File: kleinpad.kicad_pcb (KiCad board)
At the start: 2 copper layers, 25 parts, among them J1 Conn_01x02, J2 Conn_01x05, SW1 SW_Push, SW2 RotaryEncoder_Switch, U1 SuperMini nRF52840

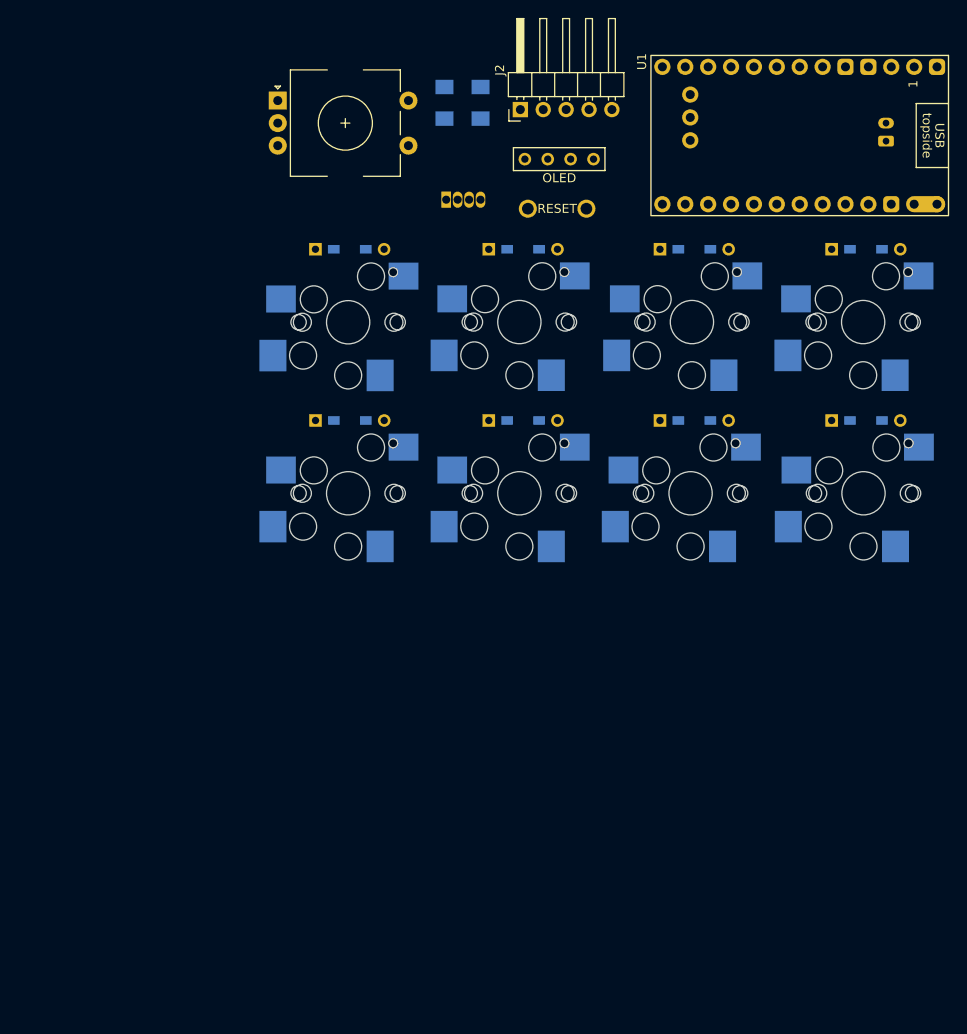
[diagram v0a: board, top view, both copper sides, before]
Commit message: feat: 回路図を追加
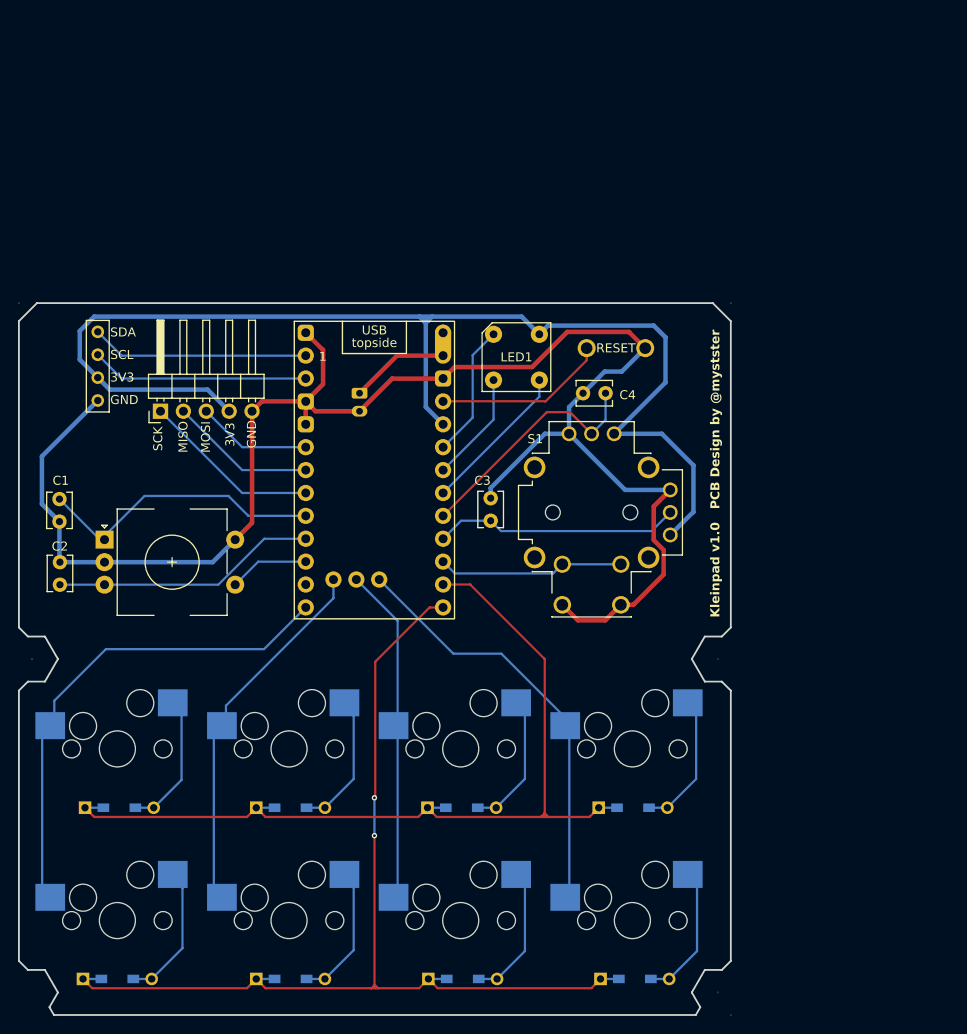
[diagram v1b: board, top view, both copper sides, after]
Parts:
- removed D9: LED_ABGR, LED_THT:LED_D5.0mm-4_RGB
- added C3: 0.1u, Capacitor_THT:C_Disc_D3.8mm_W2.6mm_P2.50mm, F.Cu at (153.6, 84.6)
- added C4: 0.1u, Capacitor_THT:C_Disc_D3.8mm_W2.6mm_P2.50mm, F.Cu at (166.4, 70.5)
- added LED1: LED_ABGR, myLibrary:LED Rectangle(OSTBMAZ2C1D), F.Cu at (156.5, 66.5)
- added S1: RKJXV122400R, RKJXV122400R:SW_RKJXV122400R, F.Cu at (164.8, 83.7)
- C1, C2: footprint kbd_Parts:Capacitor_1206 -> Capacitor_THT:C_Disc_D3.8mm_W2.6mm_P2.50mm; moved to F.Cu
- RC1-1, RC1-2, RC2-1, RC2-2, RC3-1, RC3-2, RC4-1, RC4-2: footprint kbd_SW_PCBA:MX_Choc_v1v2_Hotswap_1u -> kbd_SW:CherryMX_Hotswap_1u; moved to F.Cu
- moved C2 68.3 mm to (105.8, 91.7), turned to 90 degrees
- moved D7 67.2 mm to (169.4, 116.5)
- moved D2 67.1 mm to (112.2, 135.5)
- moved D4 67.1 mm to (131.4, 135.5)
- moved D3 67.1 mm to (131.4, 116.5)
- moved D5 67.1 mm to (150.4, 116.5)
- moved D6 67.1 mm to (150.5, 135.5)
- moved D8 67.1 mm to (169.6, 135.5)
- moved D1 67.0 mm to (112.4, 116.5)
- moved C1 65.8 mm to (105.8, 84.7), turned to 90 degrees
- moved J1 64.8 mm to (139.1, 70.5), turned to -90 degrees
- moved U1 59.9 mm to (140.7, 80.3), turned to 0 degrees
- moved OL1 58.3 mm to (110.0, 63.7), turned to -90 degrees
- moved RC4-2 53.9 mm to (169.4, 129.0), turned to 0 degrees
- moved RC1-2 53.9 mm to (112.2, 129.0), turned to 0 degrees
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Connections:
- U1 pad 10: LED_R -> RE_SW
- U1 pad 11: LED_G -> unconnected-(U1-P1.04-LF-Pad11)
- U1 pad 12: LED_B -> COL_1
- U1 pad 17: ROW_1 -> LED_R
- U1 pad 18: ROW_2 -> LED_G
- U1 pad 19: unconnected-(U1-P0.02-LF-Pad19) -> LED_B
- U1 pad 20: COL_4 -> JOY_Y
- U1 pad 21: COL_3 -> JOY_X
- U1 pad 22: COL_2 -> JOY_SW
- U1 pad 23: COL_1 -> ROW_1
- U1 pad 24: RE_SW -> ROW_2
- U1 pad 25: unconnected-(U1-P1.01-LF-Pad25) -> COL_2
- U1 pad 26: unconnected-(U1-P1.02-LF-Pad26) -> COL_3
- U1 pad 27: unconnected-(U1-P1.07-LF-Pad27) -> COL_4
- U1 pad 5: SCK -> MOSI
- U1 pad 7: MOSI -> SCK
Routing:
- net GND: track 0.00 -> 182.4 mm
- net 3V3: track 0.00 -> 136.2 mm
- net ROW_2: track 0.00 -> 115.5 mm, vias 0 -> 2
- net ROW_1: track 0.00 -> 101.3 mm
- net COL_1: track 0.00 -> 51.3 mm
- net COL_4: track 0.00 -> 47.1 mm
- net COL_2: track 0.00 -> 37.5 mm
- net COL_3: track 0.00 -> 37.2 mm
- net RE_A: track 0.00 -> 32.4 mm
- net RE_B: track 0.00 -> 29.4 mm
- net JOY_Y: track 0.00 -> 27.6 mm
- net JOY_X: track 0.00 -> 27.4 mm
- net SCL: track 0.00 -> 24.2 mm
- net SDA: track 0.00 -> 24.2 mm
- net JOY_SW: track 0.00 -> 20.7 mm
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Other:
- board outline added: 79 x 79 mm
- board text added: "3V3"
- board text added: "BAAT"
- board text added: "BAT+"
- board text added: "COL_1"
- board text added: "COL_2"
- board text added: "COL_3"
- board text added: "COL_4"
- board text added: "GND"
- board text added: "JOY_SW"
- board text added: "JOY_X"
- board text added: "JOY_Y"
- board text added: "Kleinpad v1.0 PCB Design by @mystster"
- board text added: "LED_B"
- board text added: "LED_G"
- board text added: "LED_R"
- board text added: "MISO"
- board text added: "MOSI"
- board text added: "RESET"
- board text added: "RE_A"
- board text added: "RE_B"
- board text added: "RE_SW"
- board text added: "ROW_1"
- board text added: "ROW_2"
- board text added: "SCK"
- board text added: "SCL"
- board text added: "SDA"
- board text added: "X"

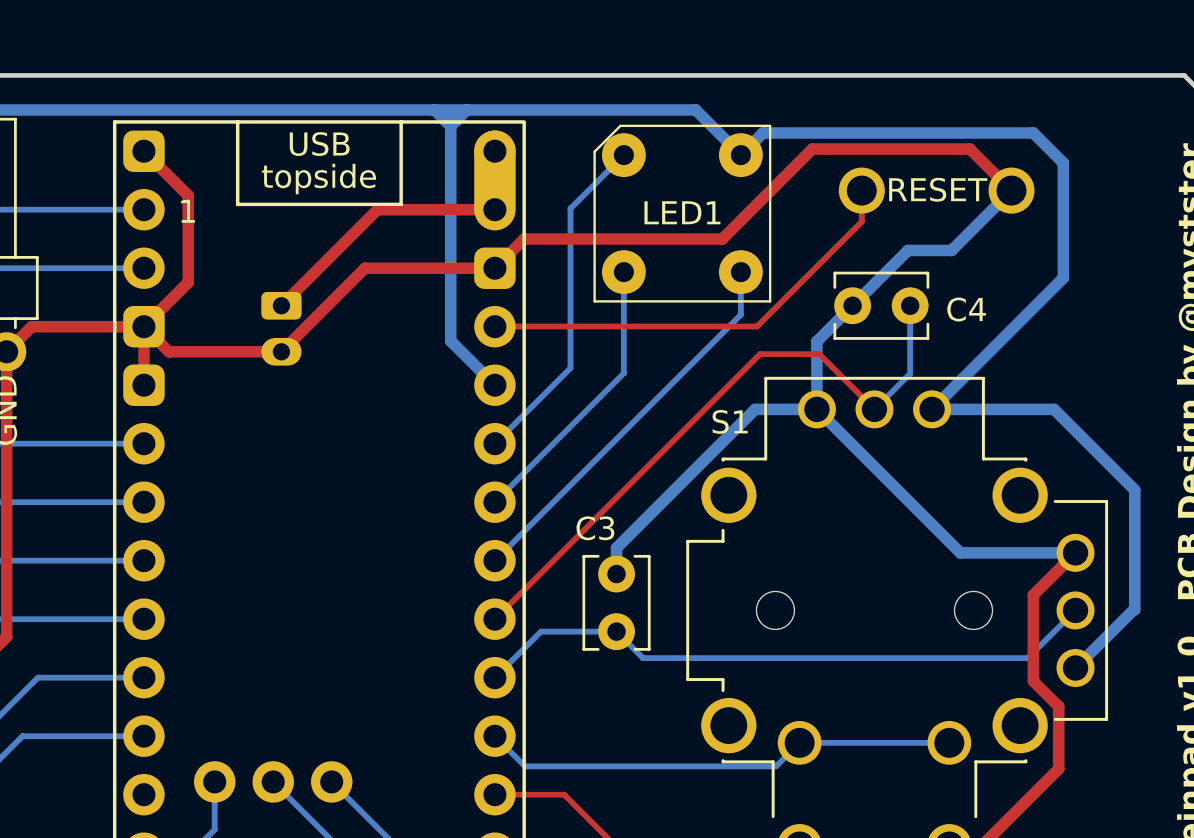
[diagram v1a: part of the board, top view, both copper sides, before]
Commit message: fix: LEDに抵抗がない
抵抗値は手元にあるものに合わせて変更
Fixes #2
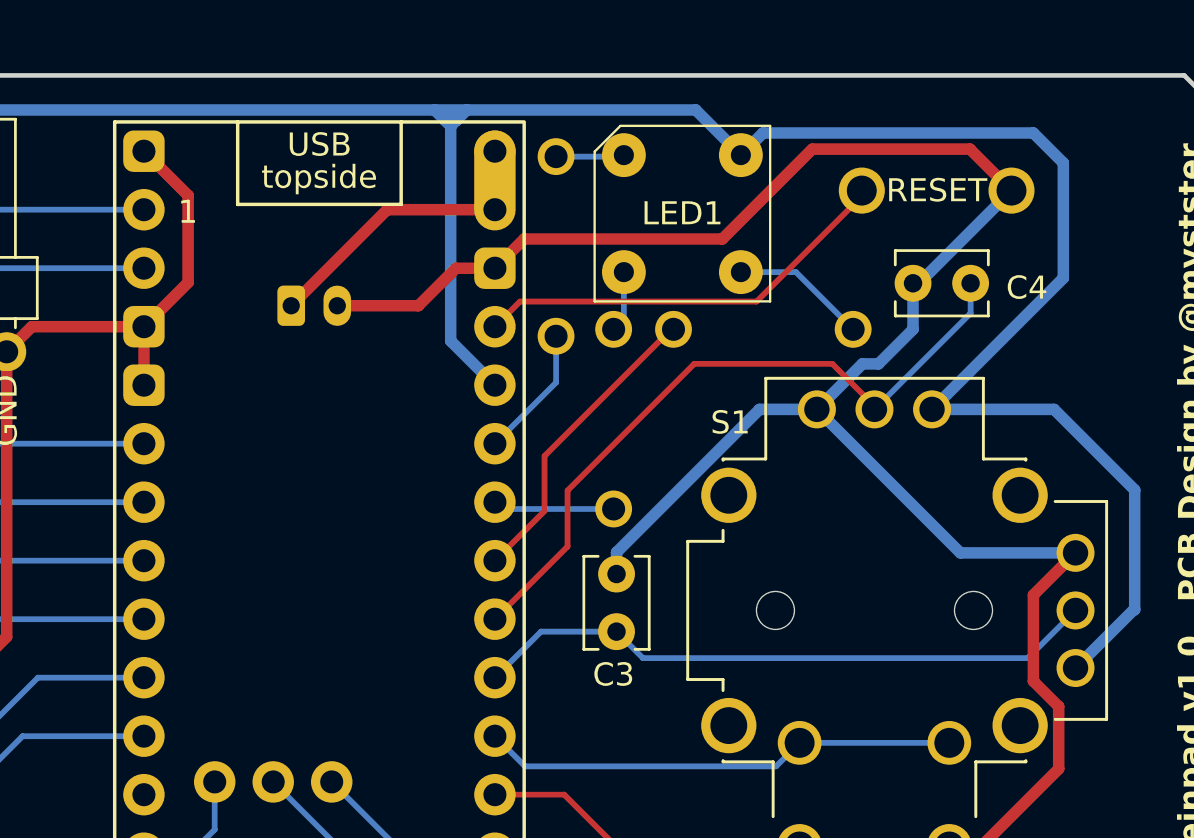
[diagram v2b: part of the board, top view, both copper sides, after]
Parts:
- added R1: 100, Keebio-Parts.pretty-master:Resistor-Compact-1-side, B.Cu at (151.0, 67.9)
- added R2: 22, Keebio-Parts.pretty-master:Resistor-Compact-1-side, B.Cu at (153.5, 75.4)
- added R3: 22, Keebio-Parts.pretty-master:Resistor-Compact-1-side, B.Cu at (160.0, 71.5)
- moved C4 2.80 mm to (169.0, 69.5)
- moved J1 0.42 mm to (139.5, 70.5), turned to 0 degrees
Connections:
- LED1 pad 2: LED_B -> Net-(LED1-BK)
- LED1 pad 3: LED_G -> Net-(LED1-GK)
- LED1 pad 4: LED_R -> Net-(LED1-RK)
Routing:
- net GND: track 182.4 -> 172.1 mm
- net LED_R: track 14.8 -> 5.76 mm
- net LED_G: track 12.3 -> 5.28 mm
- net Net-(LED1-BK): track 0.00 -> 5.90 mm
- net LED_B: track 17.0 -> 13.3 mm
- net JOY_Y: track 27.6 -> 30.8 mm
- net Net-(LED1-RK): track 0.00 -> 2.97 mm
- net Net-(LED1-GK): track 0.00 -> 2.67 mm
- net RST: track 19.2 -> 18.5 mm

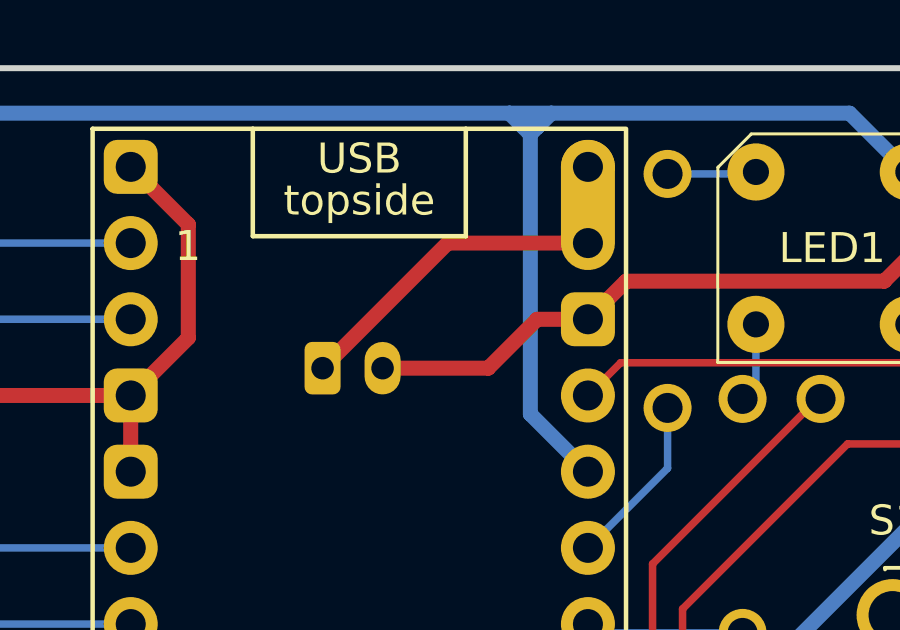
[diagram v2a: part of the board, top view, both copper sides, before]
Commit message: fix: バッテリーコネクタが接続できない Fixes #1
commit: 14f930df53bbbcb42010b72f48aa18af7e7124dd で修正済みだった
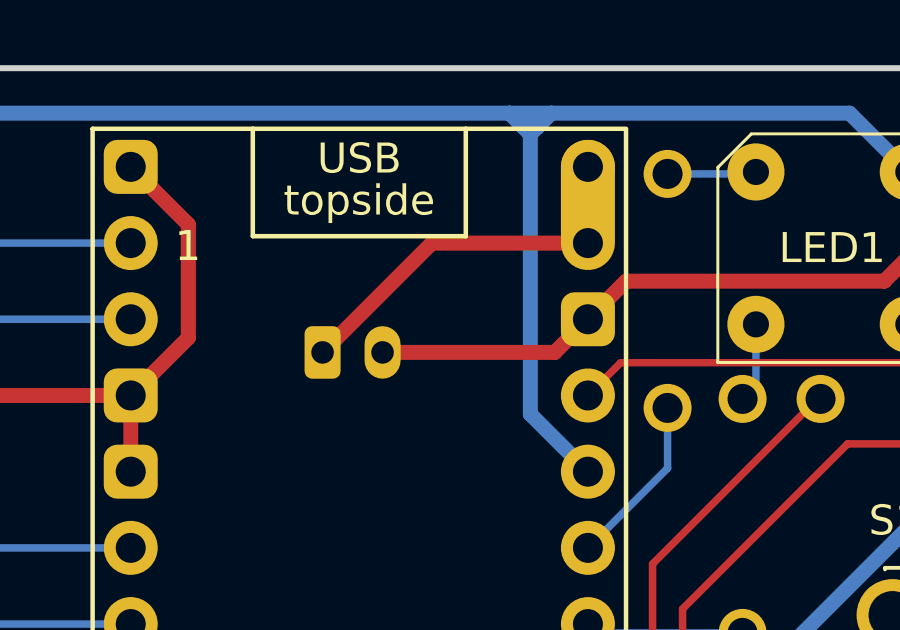
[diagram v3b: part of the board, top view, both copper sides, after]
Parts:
- moved J1 0.53 mm to (139.5, 70.0)
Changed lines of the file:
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@@
 	(footprint "Connector_JST:JST_PH_S2B-PH-K_1x02_P2.00mm_Horizontal"
 		(layer "B.Cu")
-		(at 139.5 70.4755)
+		(at 139.5 69.95)
 		(descr "JST PH series connector, S2B-PH-K (http://www.jst-mfg.com/product/pdf/eng/ePH.pdf), generated with kicad-footprint-generator")
 		(tags "connector JST PH top entry")
@@
 		(at 153.5 75.4 -90)
 		(property "Reference" "R2"
-			(at 0 -1.5 -90)
+			(at 0 -1.5 270)
 			(layer "B.SilkS")
 			(effects
@@
 		(at 160 71.5 180)
 		(property "Reference" "R3"
-			(at 0 -1.5 -0)
+			(at 0 -1.5 0)
 			(layer "B.SilkS")
 			(effects
@@
 	)
 	(segment
-		(start 146.6545 68.8455)
-		(end 145.0245 70.4755)
-		(width 0.5)
-		(layer "F.Cu")
-		(net 2)
-	)
-	(segment
 		(start 172.825625 87.8755)
 		(end 171.725625 86.7755)
@@
 	)
 	(segment
-		(start 145.0245 70.4755)
-		(end 141.5 70.4755)
+		(start 141.5 69.95)
+		(end 147.241125 69.95)
 		(width 0.5)
 		(layer "F.Cu")
@@
 	)
 	(segment
+		(start 147.241125 69.95)
+		(end 148.345625 68.8455)
+		(width 0.5)
+		(layer "F.Cu")
+		(net 2)
+	)
+	(segment
 		(start 148.345625 68.8455)
 		(end 149.615625 67.5755)
@@
 		(start 171.725625 86.7755)
 		(end 171.725625 83.0355)
-		(width 0.5)
-		(layer "F.Cu")
-		(net 2)
-	)
-	(segment
-		(start 148.345625 68.8455)
-		(end 146.6545 68.8455)
 		(width 0.5)
 		(layer "F.Cu")
@@
 	)
 	(segment
-		(start 143.67 66.3055)
-		(end 139.5 70.4755)
+		(start 143.1445 66.3055)
+		(end 139.5 69.95)
 		(width 0.5)
 		(layer "F.Cu")
@@
 	(segment
 		(start 148.345625 66.3055)
-		(end 143.67 66.3055)
-		(width 0.5)
-		(layer "F.Cu")
+		(end 143.1445 66.3055)
+		(width 0.5)
+		(layer "F.Cu")
